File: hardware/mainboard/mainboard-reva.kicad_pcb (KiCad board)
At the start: 4 copper layers, 88 x 48 mm, 77 parts, among them J1 USB-C, J2 BATTERY, J3 SM05B-GHS-TB / ENCODER, J4 SM03B-GHS-TB / SNOOZE, J5 Molex 54550-2472 / GDEY037T03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, J6 Molex 54550-0672 / FL21 front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, J7 SPEAKER, J8 SM02B-GHS-TB / WAKE_LED, Q2 AO3400A / WAKE, U1 ESP32-S3-WROOM-1-N8, U2 BQ24074RGTR, U3 TPS62840DLCR, U4 RV-3028-C7, U5 VEML7700, U6 MAX98357AETE+T, U7 USBLC6-2SC6

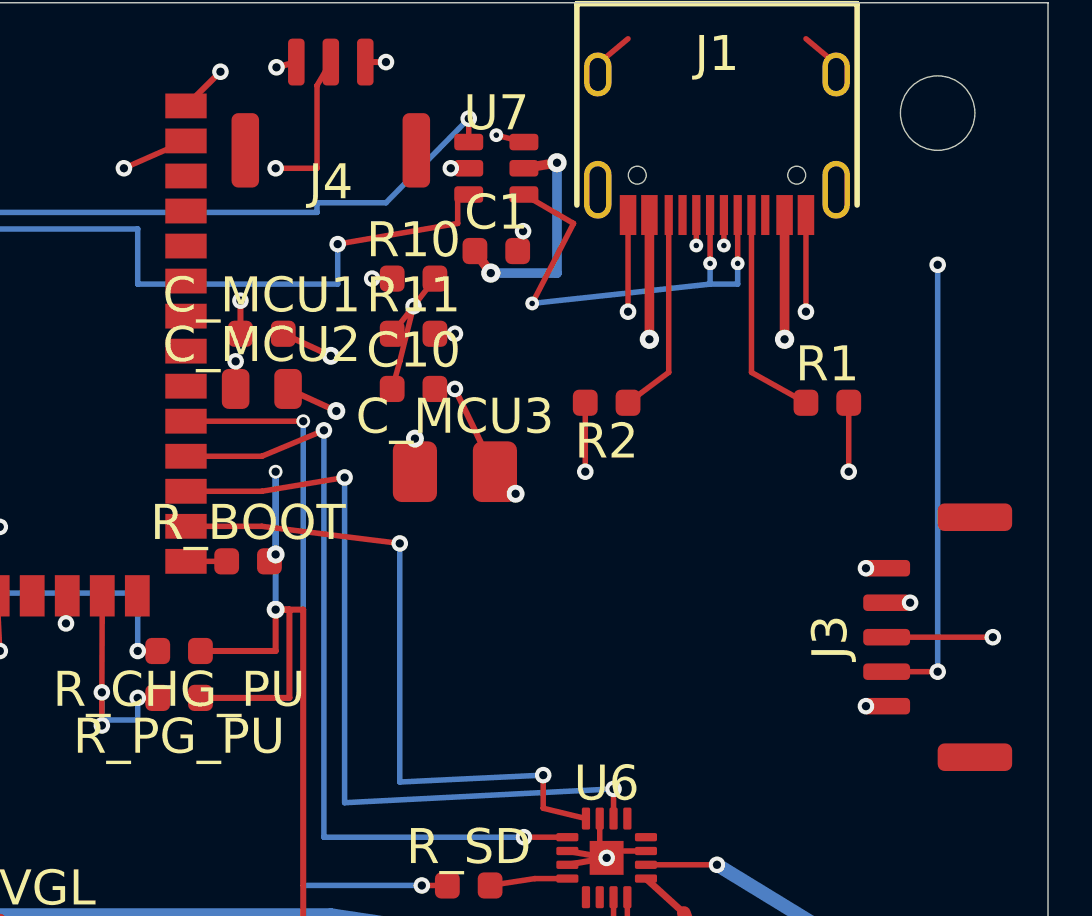
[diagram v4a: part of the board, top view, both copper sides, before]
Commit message: fix(mainboard): harden remote control inputs
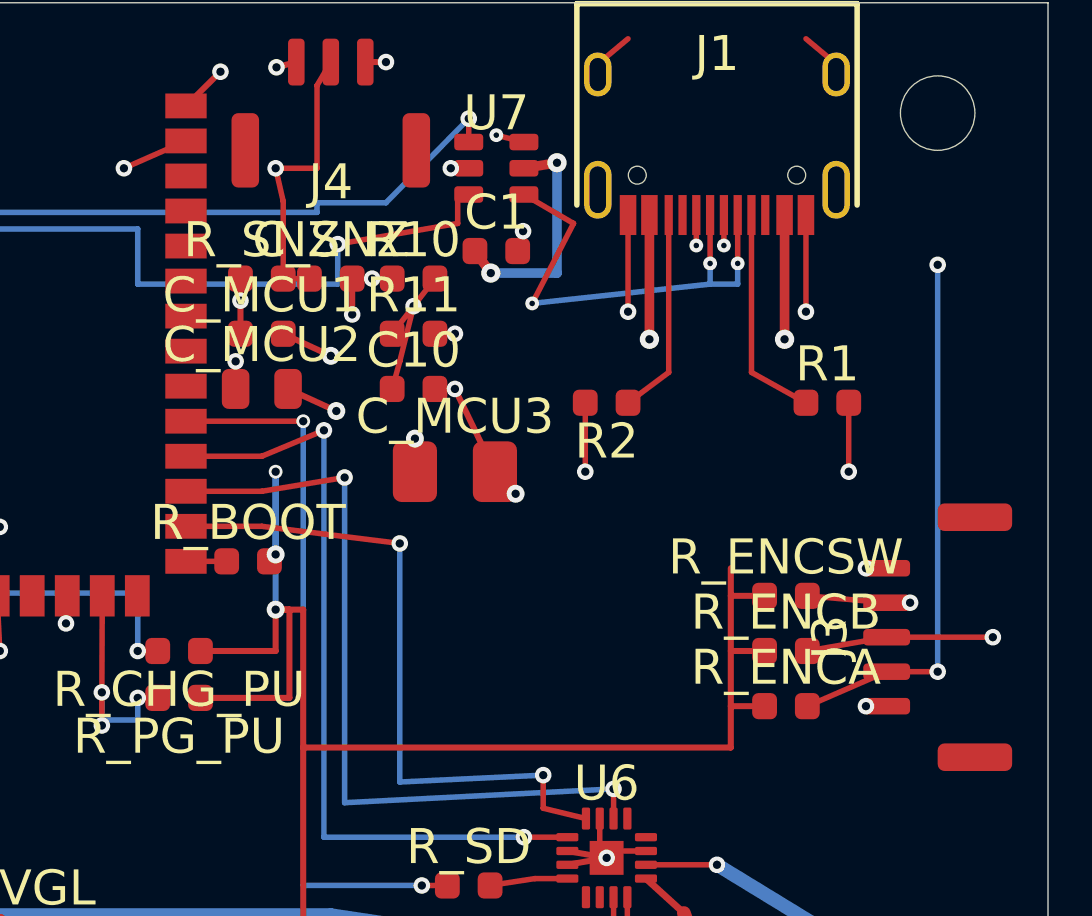
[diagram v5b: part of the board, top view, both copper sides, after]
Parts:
- added C_SNZ: 10nF, Capacitor_SMD:C_0603_1608Metric, F.Cu at (62.0, 10.0)
- added R_ENCA: 10k, Resistor_SMD:R_0603_1608Metric, F.Cu at (78.5, 25.5)
- added R_ENCB: 10k, Resistor_SMD:R_0603_1608Metric, F.Cu at (78.5, 23.5)
- added R_ENCSW: 10k, Resistor_SMD:R_0603_1608Metric, F.Cu at (78.5, 21.5)
- added R_SNZ: 10k, Resistor_SMD:R_0603_1608Metric, F.Cu at (59.5, 10.0)
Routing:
- net +3V3: track 251.6 -> 278.1 mm
- net SNOOZE_SW: track 29.1 -> 34.0 mm
- net ENC_A: track 78.3 -> 81.4 mm
- net ENC_B: track 58.7 -> 61.6 mm
- net ENC_SW: track 54.1 -> 57.0 mm
- net GND: track 112.5 -> 113.8 mm, vias 54 -> 55
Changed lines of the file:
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@@
   (segment (start 32.00 12.25) (end 32.00 13.50) (width 0.22) (layer "F.Cu") (net 1))
   (via (at 32.00 13.50) (size 0.60) (drill 0.30) (layers "F.Cu" "B.Cu") (net 1))
+  (footprint "Resistor_SMD:R_0603_1608Metric" (layer "F.Cu") (at 78.5 21.5)
+    (property "Reference" "R_ENCSW" (at 0 -1.4) (layer "F.SilkS"))
+    (property "Value" "10k" (at 0 1.4) (layer "F.Fab") hide)
+    (pad "1" smd roundrect (at -0.775 0) (size 0.9 0.95) (layers "F.Cu" "F.Paste" "F.Mask") (roundrect_rratio 0.25) (net 6 "+3V3"))
+    (pad "2" smd roundrect (at 0.775 0) (size 0.9 0.95) (layers "F.Cu" "F.Paste" "F.Mask") (roundrect_rratio 0.25) (net 46 "ENC_SW"))
+  )
+  (footprint "Resistor_SMD:R_0603_1608Metric" (layer "F.Cu") (at 78.5 23.5)
+    (property "Reference" "R_ENCB" (at 0 -1.4) (layer "F.SilkS"))
+    (property "Value" "10k" (at 0 1.4) (layer "F.Fab") hide)
+    (pad "1" smd roundrect (at -0.775 0) (size 0.9 0.95) (layers "F.Cu" "F.Paste" "F.Mask") (roundrect_rratio 0.25) (net 6 "+3V3"))
+    (pad "2" smd roundrect (at 0.775 0) (size 0.9 0.95) (layers "F.Cu" "F.Paste" "F.Mask") (roundrect_rratio 0.25) (net 45 "ENC_B"))
+  )
+  (footprint "Resistor_SMD:R_0603_1608Metric" (layer "F.Cu") (at 78.5 25.5)
+    (property "Reference" "R_ENCA" (at 0 -1.4) (layer "F.SilkS"))
+    (property "Value" "10k" (at 0 1.4) (layer "F.Fab") hide)
+    (pad "1" smd roundrect (at -0.775 0) (size 0.9 0.95) (layers "F.Cu" "F.Paste" "F.Mask") (roundrect_rratio 0.25) (net 6 "+3V3"))
+    (pad "2" smd roundrect (at 0.775 0) (size 0.9 0.95) (layers "F.Cu" "F.Paste" "F.Mask") (roundrect_rratio 0.25) (net 44 "ENC_A"))
+  )
+  (footprint "Resistor_SMD:R_0603_1608Metric" (layer "F.Cu") (at 59.5 10.0)
+    (property "Reference" "R_SNZ" (at 0 -1.4) (layer "F.SilkS"))
+    (property "Value" "10k" (at 0 1.4) (layer "F.Fab") hide)
+    (pad "1" smd roundrect (at -0.775 0) (size 0.9 0.95) (layers "F.Cu" "F.Paste" "F.Mask") (roundrect_rratio 0.25) (net 6 "+3V3"))
+    (pad "2" smd roundrect (at 0.775 0) (size 0.9 0.95) (layers "F.Cu" "F.Paste" "F.Mask") (roundrect_rratio 0.25) (net 43 "SNOOZE_SW"))
+  )
+  (footprint "Capacitor_SMD:C_0603_1608Metric" (layer "F.Cu") (at 62.0 10.0)
+    (property "Reference" "C_SNZ" (at 0 -1.4) (layer "F.SilkS"))
+    (property "Value" "10nF" (at 0 1.4) (layer "F.Fab") hide)
+    (pad "1" smd roundrect (at -0.775 0) (size 0.9 0.95) (layers "F.Cu" "F.Paste" "F.Mask") (roundrect_rratio 0.25) (net 43 "SNOOZE_SW"))
+    (pad "2" smd roundrect (at 0.775 0) (size 0.9 0.95) (layers "F.Cu" "F.Paste" "F.Mask") (roundrect_rratio 0.25) (net 1 "GND"))
+  )
+  (segment (start 61.0 27.0) (end 76.5 27.0) (width 0.22) (layer "F.Cu") (net 6))
+  (segment (start 76.5 27.0) (end 76.5 20.5) (width 0.22) (layer "F.Cu") (net 6))
+  (segment (start 76.5 21.5) (end 77.725 21.5) (width 0.22) (layer "F.Cu") (net 6))
+  (segment (start 76.5 23.5) (end 77.725 23.5) (width 0.22) (layer "F.Cu") (net 6))
+  (segment (start 76.5 25.5) (end 77.725 25.5) (width 0.22) (layer "F.Cu") (net 6))
+  (segment (start 79.275 21.5) (end 82.15 21.75) (width 0.20) (layer "F.Cu") (net 46))
+  (segment (start 79.275 23.5) (end 82.15 23.0) (width 0.20) (layer "F.Cu") (net 45))
+  (segment (start 79.275 25.5) (end 82.15 24.25) (width 0.20) (layer "F.Cu") (net 44))
+  (segment (start 58.725 10.0) (end 58.725 10.8) (width 0.22) (layer "F.Cu") (net 6))
+  (segment (start 60.275 10.0) (end 61.225 10.0) (width 0.20) (layer "F.Cu") (net 43))
+  (segment (start 60.275 10.0) (end 60.275 7.2) (width 0.20) (layer "F.Cu") (net 43))
+  (segment (start 60.275 7.2) (end 60.0 6.0) (width 0.20) (layer "F.Cu") (net 43))
+  (segment (start 62.775 10.0) (end 62.775 11.3) (width 0.22) (layer "F.Cu") (net 1))
+  (via (at 62.775 11.3) (size 0.60) (drill 0.30) (layers "F.Cu" "B.Cu") (net 1))
 )

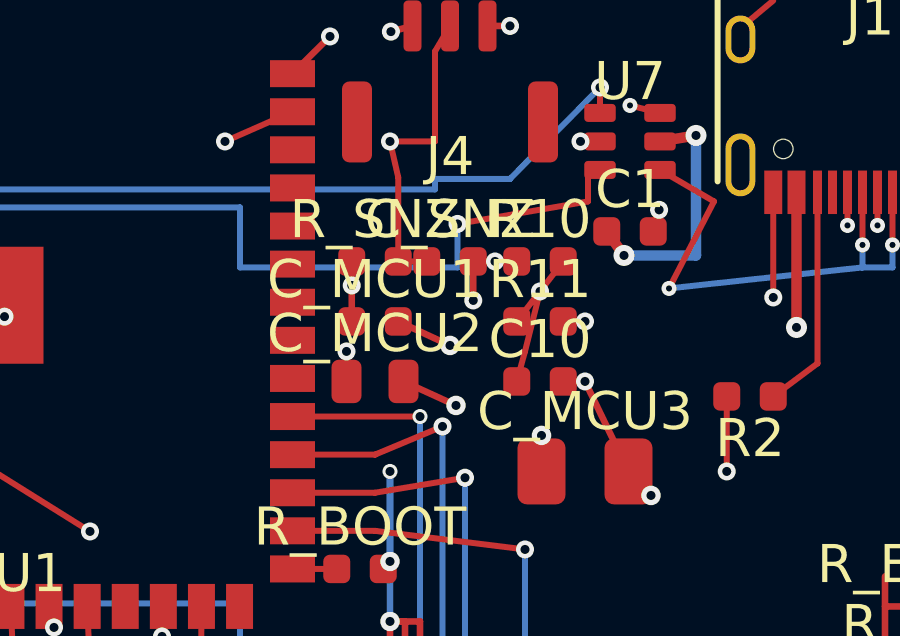
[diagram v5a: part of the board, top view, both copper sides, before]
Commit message: fix(mainboard): clear Snooze RC DRC conflicts
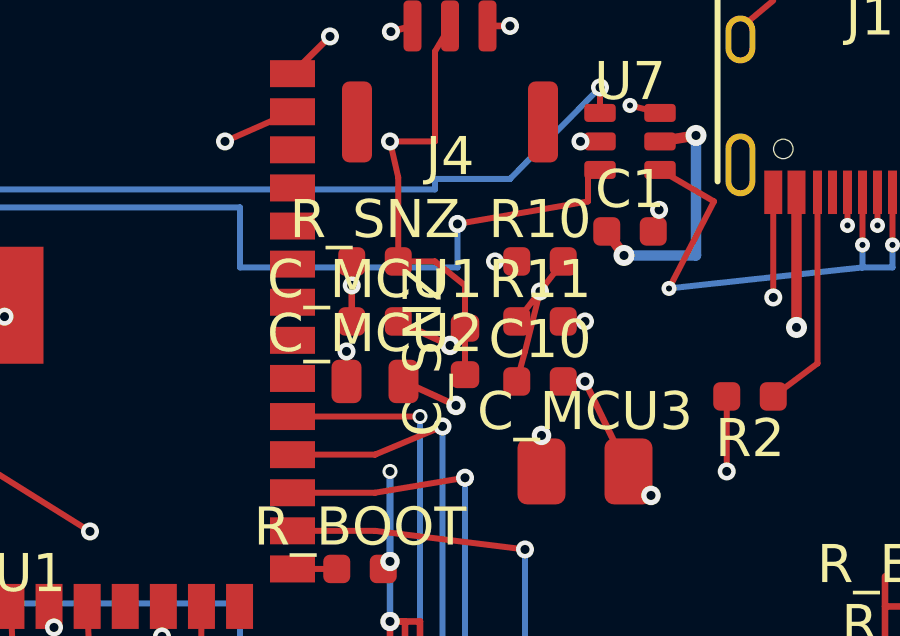
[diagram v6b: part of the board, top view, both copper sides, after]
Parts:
- moved C_SNZ 3.04 mm to (62.5, 13.0), turned to 90 degrees
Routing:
- net SNOOZE_SW: track 34.0 -> 38.6 mm
- net GND: track 113.8 -> 113.2 mm, vias 55 -> 54
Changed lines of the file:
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@@
     (pad "2" smd roundrect (at 0.775 0) (size 0.9 0.95) (layers "F.Cu" "F.Paste" "F.Mask") (roundrect_rratio 0.25) (net 43 "SNOOZE_SW"))
   )
-  (footprint "Capacitor_SMD:C_0603_1608Metric" (layer "F.Cu") (at 62.0 10.0)
-    (property "Reference" "C_SNZ" (at 0 -1.4) (layer "F.SilkS"))
-    (property "Value" "10nF" (at 0 1.4) (layer "F.Fab") hide)
-    (pad "1" smd roundrect (at -0.775 0) (size 0.9 0.95) (layers "F.Cu" "F.Paste" "F.Mask") (roundrect_rratio 0.25) (net 43 "SNOOZE_SW"))
-    (pad "2" smd roundrect (at 0.775 0) (size 0.9 0.95) (layers "F.Cu" "F.Paste" "F.Mask") (roundrect_rratio 0.25) (net 1 "GND"))
+  (footprint "Capacitor_SMD:C_0603_1608Metric" (layer "F.Cu") (at 62.5 13.0 90)
+    (property "Reference" "C_SNZ" (at 0 -1.4 90) (layer "F.SilkS"))
+    (property "Value" "10nF" (at 0 1.4 90) (layer "F.Fab") hide)
+    (pad "1" smd roundrect (at -0.775 0 90) (size 0.9 0.95) (layers "F.Cu" "F.Paste" "F.Mask") (roundrect_rratio 0.25) (net 43 "SNOOZE_SW"))
+    (pad "2" smd roundrect (at 0.775 0 90) (size 0.9 0.95) (layers "F.Cu" "F.Paste" "F.Mask") (roundrect_rratio 0.25) (net 1 "GND"))
   )
   (segment (start 61.0 27.0) (end 76.5 27.0) (width 0.22) (layer "F.Cu") (net 6))
@@
   (segment (start 79.275 25.5) (end 82.15 24.25) (width 0.20) (layer "F.Cu") (net 44))
   (segment (start 58.725 10.0) (end 58.725 10.8) (width 0.22) (layer "F.Cu") (net 6))
-  (segment (start 60.275 10.0) (end 61.225 10.0) (width 0.20) (layer "F.Cu") (net 43))
+  (segment (start 60.275 10.0) (end 61.5 10.0) (width 0.20) (layer "F.Cu") (net 43))
+  (segment (start 61.5 10.0) (end 62.5 10.8) (width 0.20) (layer "F.Cu") (net 43))
+  (segment (start 62.5 10.8) (end 62.5 13.775) (width 0.20) (layer "F.Cu") (net 43))
+  (segment (start 62.5 12.225) (end 62.0 12.8) (width 0.22) (layer "F.Cu") (net 1))
   (segment (start 60.275 10.0) (end 60.275 7.2) (width 0.20) (layer "F.Cu") (net 43))
   (segment (start 60.275 7.2) (end 60.0 6.0) (width 0.20) (layer "F.Cu") (net 43))
-  (segment (start 62.775 10.0) (end 62.775 11.3) (width 0.22) (layer "F.Cu") (net 1))
-  (via (at 62.775 11.3) (size 0.60) (drill 0.30) (layers "F.Cu" "B.Cu") (net 1))
 )

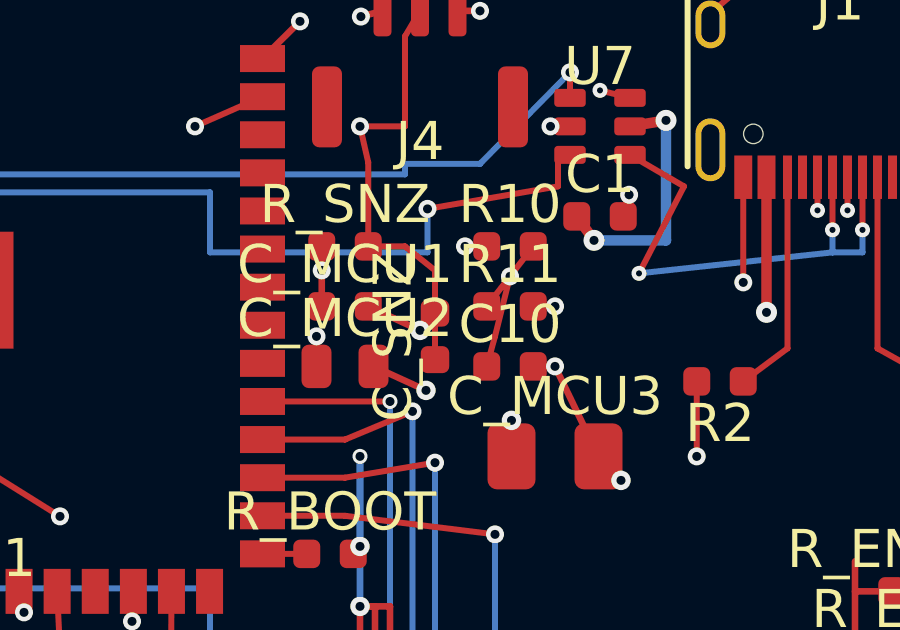
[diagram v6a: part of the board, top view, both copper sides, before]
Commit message: fix(mainboard): route Snooze around RC ground pad
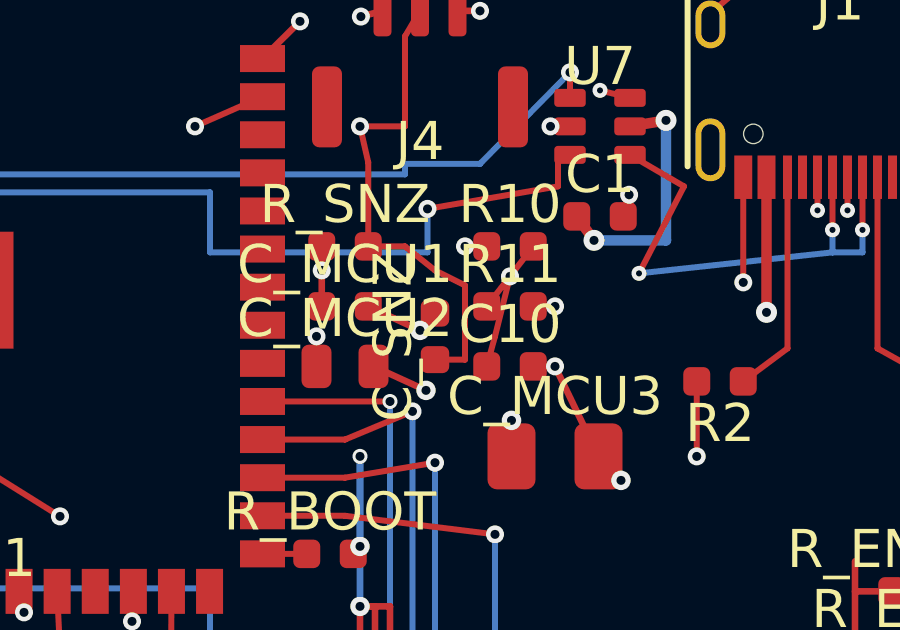
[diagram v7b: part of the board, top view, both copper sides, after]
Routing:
- net SNOOZE_SW: track 38.6 -> 40.2 mm
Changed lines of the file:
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@@
   (segment (start 60.275 10.0) (end 61.5 10.0) (width 0.20) (layer "F.Cu") (net 43))
   (segment (start 61.5 10.0) (end 62.5 10.8) (width 0.20) (layer "F.Cu") (net 43))
-  (segment (start 62.5 10.8) (end 62.5 13.775) (width 0.20) (layer "F.Cu") (net 43))
+  (segment (start 62.5 10.8) (end 63.5 11.3) (width 0.20) (layer "F.Cu") (net 43))
+  (segment (start 63.5 11.3) (end 63.5 13.775) (width 0.20) (layer "F.Cu") (net 43))
+  (segment (start 63.5 13.775) (end 62.5 13.775) (width 0.20) (layer "F.Cu") (net 43))
   (segment (start 62.5 12.225) (end 62.0 12.8) (width 0.22) (layer "F.Cu") (net 1))
   (segment (start 60.275 10.0) (end 60.275 7.2) (width 0.20) (layer "F.Cu") (net 43))

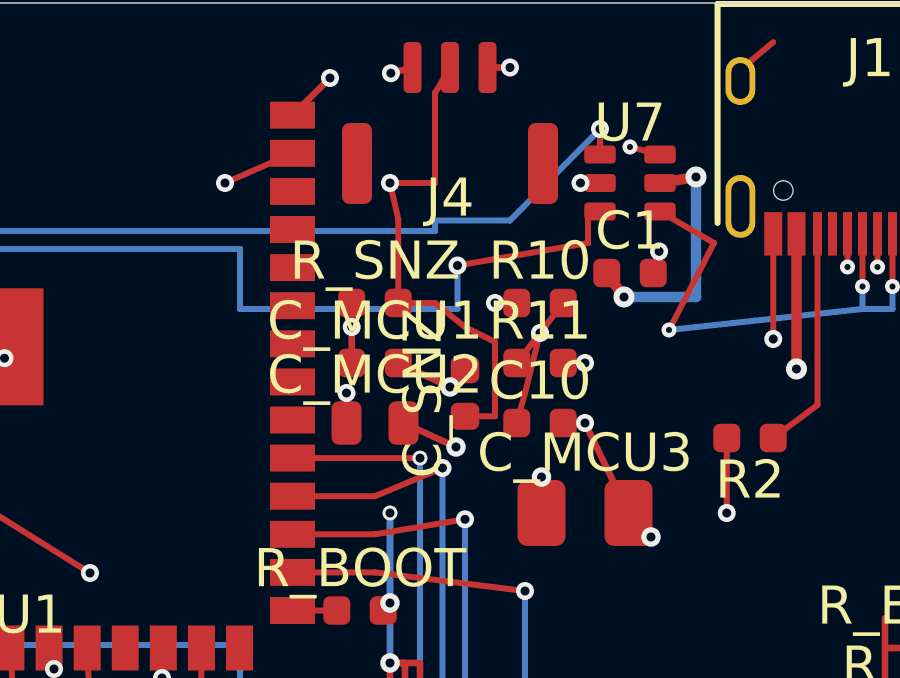
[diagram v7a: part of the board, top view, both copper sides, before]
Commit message: fix(mainboard): relocate Snooze filter below J4
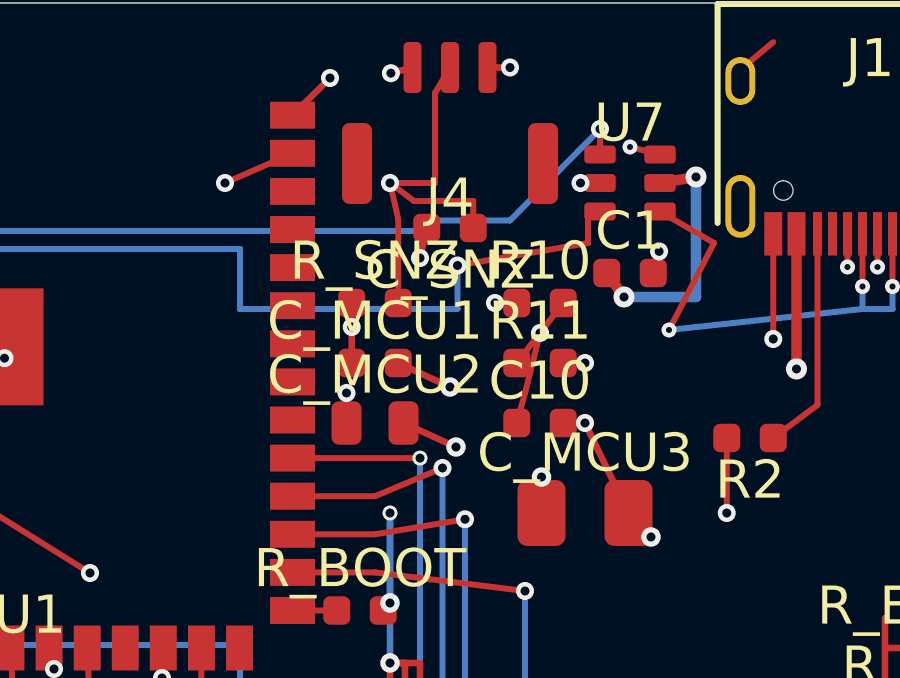
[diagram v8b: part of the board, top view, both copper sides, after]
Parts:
- moved C_SNZ 5.52 mm to (62.0, 7.50), turned to 180 degrees
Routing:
- net SNOOZE_SW: track 40.2 -> 37.0 mm
- net GND: track 113.2 -> 113.5 mm, vias 54 -> 55
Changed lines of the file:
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@@
     (pad "2" smd roundrect (at 0.775 0) (size 0.9 0.95) (layers "F.Cu" "F.Paste" "F.Mask") (roundrect_rratio 0.25) (net 43 "SNOOZE_SW"))
   )
-  (footprint "Capacitor_SMD:C_0603_1608Metric" (layer "F.Cu") (at 62.5 13.0 90)
-    (property "Reference" "C_SNZ" (at 0 -1.4 90) (layer "F.SilkS"))
-    (property "Value" "10nF" (at 0 1.4 90) (layer "F.Fab") hide)
-    (pad "1" smd roundrect (at -0.775 0 90) (size 0.9 0.95) (layers "F.Cu" "F.Paste" "F.Mask") (roundrect_rratio 0.25) (net 43 "SNOOZE_SW"))
-    (pad "2" smd roundrect (at 0.775 0 90) (size 0.9 0.95) (layers "F.Cu" "F.Paste" "F.Mask") (roundrect_rratio 0.25) (net 1 "GND"))
+  (footprint "Capacitor_SMD:C_0603_1608Metric" (layer "F.Cu") (at 62.0 7.5 180)
+    (property "Reference" "C_SNZ" (at 0 -1.4 180) (layer "F.SilkS"))
+    (property "Value" "10nF" (at 0 1.4 180) (layer "F.Fab") hide)
+    (pad "1" smd roundrect (at -0.775 0 180) (size 0.9 0.95) (layers "F.Cu" "F.Paste" "F.Mask") (roundrect_rratio 0.25) (net 43 "SNOOZE_SW"))
+    (pad "2" smd roundrect (at 0.775 0 180) (size 0.9 0.95) (layers "F.Cu" "F.Paste" "F.Mask") (roundrect_rratio 0.25) (net 1 "GND"))
   )
   (segment (start 61.0 27.0) (end 76.5 27.0) (width 0.22) (layer "F.Cu") (net 6))
@@
   (segment (start 79.275 25.5) (end 82.15 24.25) (width 0.20) (layer "F.Cu") (net 44))
   (segment (start 58.725 10.0) (end 58.725 10.8) (width 0.22) (layer "F.Cu") (net 6))
-  (segment (start 60.275 10.0) (end 61.5 10.0) (width 0.20) (layer "F.Cu") (net 43))
-  (segment (start 61.5 10.0) (end 62.5 10.8) (width 0.20) (layer "F.Cu") (net 43))
-  (segment (start 62.5 10.8) (end 63.5 11.3) (width 0.20) (layer "F.Cu") (net 43))
-  (segment (start 63.5 11.3) (end 63.5 13.775) (width 0.20) (layer "F.Cu") (net 43))
-  (segment (start 63.5 13.775) (end 62.5 13.775) (width 0.20) (layer "F.Cu") (net 43))
-  (segment (start 62.5 12.225) (end 62.0 12.8) (width 0.22) (layer "F.Cu") (net 1))
+  (segment (start 62.775 7.5) (end 62.775 6.6) (width 0.20) (layer "F.Cu") (net 43))
+  (segment (start 62.775 6.6) (end 60.8 6.6) (width 0.20) (layer "F.Cu") (net 43))
+  (segment (start 60.8 6.6) (end 60.0 6.0) (width 0.20) (layer "F.Cu") (net 43))
+  (segment (start 61.225 7.5) (end 61.0 8.5) (width 0.22) (layer "F.Cu") (net 1))
+  (via (at 61.0 8.5) (size 0.60) (drill 0.30) (layers "F.Cu" "B.Cu") (net 1))
   (segment (start 60.275 10.0) (end 60.275 7.2) (width 0.20) (layer "F.Cu") (net 43))
   (segment (start 60.275 7.2) (end 60.0 6.0) (width 0.20) (layer "F.Cu") (net 43))
